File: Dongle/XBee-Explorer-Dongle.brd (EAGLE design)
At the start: 40.6 x 27.9 mm, 38 parts, among them U2 XBEE-1B3, U3 MIC5205 3.3V, U4 FT231XS

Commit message: Increasing fiducial size and LED footprint
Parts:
- removed LED1: Red, SparkFun:LED-0603
- removed LED2: Red-TX, SparkFun:LED-0603
- removed LED3: Green-RX, SparkFun:LED-0603
- removed LED4: Green, SparkFun:LED-0603
- added D1, D4: RED, SparkFun-LED:LED-0603
- added D2, D3: GREEN, SparkFun-LED:LED-0603
- FID1, FID2: value FIDUCIALUFIDUCIAL -> FIDUCIAL1X2; device SparkFun-Aesthetics:MICRO-FIDUCIAL -> SparkFun-Aesthetics:FIDUCIAL-1X2
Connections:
- net GND: now also D3.C, D4.C; no longer LED1.C, LED4.C
- net N$1: now also D1.A; no longer LED2.A
- net N$2: now also D3.A; no longer LED4.A
- net N$38: now also D4.A; no longer LED1.A
- net N$4: now also D2.A; no longer LED3.A
- net RXLED: now also D2.C; no longer LED3.C
- net TXLED: now also D1.C; no longer LED2.C
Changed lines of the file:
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@@
 <wire x1="0" y1="27.94" x2="40.64" y2="27.94" width="0.2032" layer="20"/>
 <wire x1="0" y1="0" x2="40.64" y2="0" width="0.2032" layer="20"/>
-<text x="7.62" y="17.272" size="1.016" layer="21" ratio="15">PWR</text>
-<text x="37.592" y="9.525" size="1.016" layer="21" ratio="15" align="center-right">TX</text>
-<text x="37.592" y="8.255" size="1.016" layer="21" ratio="15" align="center-right">RX</text>
-<text x="37.592" y="19.685" size="1.016" layer="21" ratio="15" align="center-right">RSSI</text>
+<text x="9.017" y="17.78" size="1.016" layer="21" ratio="15" align="center">PWR</text>
+<text x="37.338" y="9.525" size="1.016" layer="21" ratio="15" align="center-right">TX</text>
+<text x="37.338" y="8.255" size="1.016" layer="21" ratio="15" align="center-right">RX</text>
+<text x="37.338" y="19.685" size="1.016" layer="21" ratio="15" align="center-right">RSSI</text>
 <text x="33.528" y="20.066" size="1.016" layer="22" ratio="15" rot="MR270">3.3V</text>
 <text x="30.988" y="20.066" size="1.016" layer="22" ratio="15" rot="MR270">DOUT</text>
@@
 </class>
 </classes>
-<designrules name="SparkFun">
+<designrules name="SparkFun-2-layer">
 <description language="en">&lt;b&gt;EAGLE Design Rules&lt;/b&gt;
 &lt;p&gt;
@@
 <param name="dpGapFactor" value="2.5"/>
 <param name="checkGrid" value="0"/>
-<param name="checkAngle" value="0"/>
+<param name="checkAngle" value="1"/>
 <param name="checkFont" value="1"/>
 <param name="checkRestrict" value="1"/>
@@
 <attribute name="VALUE" x="19.8755" y="8.636" size="0.4064" layer="27"/>
 </element>
-<element name="LED1" library="SparkFun" package="LED-0603" value="Red" x="8.89" y="19.05" smashed="yes" rot="R90">
-<attribute name="NAME" x="9.779" y="18.3515" size="0.4064" layer="25" rot="R180"/>
-<attribute name="VALUE" x="10.287" y="18.3515" size="0.4064" layer="27"/>
-</element>
-<element name="LED2" library="SparkFun" package="LED-0603" value="Red-TX" x="38.735" y="9.525" smashed="yes" rot="R270">
-<attribute name="NAME" x="36.735" y="9.525" size="1.27" layer="25" rot="R180"/>
-<attribute name="VALUE" x="38.163" y="8.89" size="0.4064" layer="27" rot="R180"/>
-</element>
-<element name="LED3" library="SparkFun" package="LED-0603" value="Green-RX" x="38.735" y="8.255" smashed="yes" rot="R270">
-<attribute name="NAME" x="36.735" y="8.255" size="1.27" layer="25" rot="R180"/>
-<attribute name="VALUE" x="38.163" y="7.493" size="0.4064" layer="27" rot="R180"/>
-</element>
 <element name="R1" library="SparkFun" package="0603-RES" value="1K" x="31.75" y="10.414" smashed="yes">
 <attribute name="NAME" x="33.75" y="10.414" size="1.27" layer="25"/>
@@
 <element name="U$10" library="SparkFun" package="STAND-OFF" value="STAND-OFF" x="38.1" y="25.4"/>
 <element name="U$11" library="SparkFun" package="STAND-OFF" value="STAND-OFF" x="38.1" y="2.54"/>
-<element name="LED4" library="SparkFun" package="LED-0603" value="Green" x="38.735" y="19.685" smashed="yes" rot="R270">
-<attribute name="NAME" x="37.846" y="20.3835" size="0.4064" layer="25"/>
-<attribute name="VALUE" x="36.068" y="18.4785" size="0.4064" layer="27"/>
-</element>
 <element name="R4" library="SparkFun" package="0603-RES" value="330" x="22.86" y="19.05" smashed="yes" rot="R180">
 <attribute name="NAME" x="23.749" y="18.3515" size="0.4064" layer="25" rot="R180"/>
@@
 <element name="FRAME1" library="SparkFun-Aesthetics" package="CREATIVE_COMMONS" value="FRAME-LETTER" x="6.35" y="-8.89"/>
 <element name="U$7" library="SparkFun" package="OSHW-LOGO-S" value="OSHW-LOGOS" x="8.89" y="25.4"/>
-<element name="FID1" library="SparkFun-Aesthetics" package="MICRO-FIDUCIAL" value="FIDUCIALUFIDUCIAL" x="6.35" y="26.67"/>
-<element name="FID2" library="SparkFun-Aesthetics" package="MICRO-FIDUCIAL" value="FIDUCIALUFIDUCIAL" x="34.29" y="1.27"/>
-<element name="S2" library="SparkFun-Electromechanical" package="TACTILE_SWITCH_SMD" value="Reset" x="37.973" y="13.97" rot="R270"/>
+<element name="FID1" library="SparkFun-Aesthetics" package="FIDUCIAL-1X2" value="FIDUCIAL1X2" x="6.35" y="26.67"/>
+<element name="FID2" library="SparkFun-Aesthetics" package="FIDUCIAL-1X2" value="FIDUCIAL1X2" x="34.29" y="1.27"/>
+<element name="S2" library="SparkFun-Electromechanical" package="TACTILE_SWITCH_SMD" value="Reset" x="37.973" y="13.97" rot="R270">
+<attribute name="PROD_ID" value="SWCH-08247" x="37.973" y="13.97" size="1.778" layer="27" rot="R270" display="off"/>
+</element>
 <element name="U2" library="SparkFun-RF" package="XBEE-SMD" value="XBEE-1B3" x="11.43" y="13.97" rot="R270">
 <attribute name="PROD_ID" value="CONN-09042" x="11.43" y="13.97" size="1.27" layer="27" font="vector" ratio="15" rot="R270" display="off"/>
@@
 <element name="SJ3" library="SparkFun-Passives" package="SJ_2S-TRACE" value="RSSI" x="16.51" y="3.81" rot="MR0"/>
 <element name="SJ4" library="SparkFun-Passives" package="SJ_2S-TRACE" value="RSSI" x="13.97" y="24.13" rot="MR0"/>
+<element name="D1" library="SparkFun-LED" package="LED-0603" value="RED" x="38.735" y="9.525" rot="R270">
+<attribute name="PROD_ID" value="DIO-00819" x="38.735" y="9.525" size="1.778" layer="27" font="vector" ratio="15" rot="R270" display="off"/>
+</element>
+<element name="D2" library="SparkFun-LED" package="LED-0603" value="GREEN" x="38.735" y="8.255" rot="R270">
+<attribute name="PROD_ID" value="DIO-00821" x="38.735" y="8.255" size="1.778" layer="27" font="vector" ratio="15" rot="R270" display="off"/>
+</element>
+<element name="D3" library="SparkFun-LED" package="LED-0603" value="GREEN" x="38.735" y="19.685" rot="R270">
+<attribute name="PROD_ID" value="DIO-00821" x="38.735" y="19.685" size="1.778" layer="27" font="vector" ratio="15" rot="R270" display="off"/>
+</element>
+<element name="D4" library="SparkFun-LED" package="LED-0603" value="RED" x="8.89" y="19.05" rot="R90">
+<attribute name="PROD_ID" value="DIO-00819" x="8.89" y="19.05" size="1.778" layer="27" font="vector" ratio="15" rot="R90" display="off"/>
+</element>
 </elements>
 <signals>
@@
 <contactref element="C11" pad="2"/>
 <contactref element="C14" pad="2"/>
-<contactref element="LED1" pad="C"/>
-<contactref element="LED4" pad="C"/>
 <contactref element="U3" pad="2"/>
 <contactref element="C1" pad="C"/>
@@
 <contactref element="U2" pad="10"/>
 <contactref element="U2" pad="10"/>
+<contactref element="D4" pad="C"/>
+<contactref element="D3" pad="C"/>
 </signal>
 <signal name="RESET">
@@
 <signal name="N$38">
 <contactref element="R11" pad="1"/>
-<contactref element="LED1" pad="A"/>
-<wire x1="9.64" y1="19.05" x2="11.85" y2="19.05" width="0.254" layer="1"/>
+<contactref element="D4" pad="A"/>
+<wire x1="9.767" y1="19.05" x2="11.85" y2="19.05" width="0.254" layer="1"/>
 </signal>
 <signal name="N$1">
-<contactref element="LED2" pad="A"/>
 <contactref element="R1" pad="2"/>
 <wire x1="32.6" y1="10.414" x2="35.306" y2="10.414" width="0.254" layer="1"/>
 <wire x1="35.306" y1="10.414" x2="36.195" y2="9.525" width="0.254" layer="1"/>
-<wire x1="37.985" y1="9.525" x2="36.195" y2="9.525" width="0.254" layer="1"/>
+<contactref element="D1" pad="A"/>
+<wire x1="36.195" y1="9.525" x2="37.858" y2="9.525" width="0.254" layer="1"/>
 </signal>
 <signal name="N$4">
-<contactref element="LED3" pad="A"/>
 <contactref element="R3" pad="2"/>
 <wire x1="32.6" y1="8.636" x2="35.814" y2="8.636" width="0.254" layer="1"/>
 <wire x1="35.814" y1="8.636" x2="36.195" y2="8.255" width="0.254" layer="1"/>
-<wire x1="37.985" y1="8.255" x2="36.195" y2="8.255" width="0.254" layer="1"/>
+<contactref element="D2" pad="A"/>
+<wire x1="36.195" y1="8.255" x2="37.858" y2="8.255" width="0.254" layer="1"/>
 </signal>
 <signal name="DIN">
@@
 </signal>
 <signal name="TXLED">
-<contactref element="LED2" pad="C"/>
 <via x="38.1" y="11.43" extent="1-16" drill="0.508"/>
 <contactref element="U4" pad="10"/>
@@
 <wire x1="22.86" y1="15.24" x2="34.29" y2="15.24" width="0.254" layer="16"/>
 <wire x1="34.29" y1="15.24" x2="38.1" y2="11.43" width="0.254" layer="16"/>
-<wire x1="39.485" y1="9.525" x2="39.497" y2="10.033" width="0.254" layer="1"/>
-<wire x1="39.497" y1="10.033" x2="38.1" y2="11.43" width="0.254" layer="1"/>
+<contactref element="D1" pad="C"/>
+<wire x1="39.612" y1="9.525" x2="39.612" y2="9.918" width="0.254" layer="1"/>
+<wire x1="39.612" y1="9.918" x2="38.1" y2="11.43" width="0.254" layer="1"/>
 </signal>
 <signal name="RXLED">
-<contactref element="LED3" pad="C"/>
 <contactref element="U4" pad="17"/>
 <wire x1="23.8125" y1="11.2903" x2="23.8125" y2="10.6045" width="0.254" layer="1"/>
@@
 <wire x1="37.973" y1="7.747" x2="39.37" y2="6.35" width="0.254" layer="16"/>
 <via x="39.37" y="6.35" extent="1-16" drill="0.508"/>
-<wire x1="39.37" y1="6.35" x2="39.37" y2="8.14" width="0.254" layer="1"/>
-<wire x1="39.37" y1="8.14" x2="39.485" y2="8.255" width="0.254" layer="1"/>
+<contactref element="D2" pad="C"/>
+<wire x1="39.612" y1="8.255" x2="39.612" y2="7.481" width="0.254" layer="1"/>
+<wire x1="39.612" y1="7.481" x2="39.37" y2="7.239" width="0.254" layer="1"/>
+<wire x1="39.37" y1="7.239" x2="39.37" y2="6.35" width="0.254" layer="1"/>
 </signal>
 <signal name="DIO4">
@@
 </signal>
 <signal name="N$2">
-<contactref element="LED4" pad="A"/>
 <contactref element="R4" pad="1"/>
 <wire x1="23.71" y1="19.05" x2="24.511" y2="19.05" width="0.254" layer="1"/>
@@
 <via x="28.829" y="19.939" extent="1-16" drill="0.508"/>
 <via x="37.973" y="20.955" extent="1-16" drill="0.508"/>
-<wire x1="37.985" y1="19.685" x2="37.973" y2="20.955" width="0.254" layer="1"/>
 <wire x1="28.829" y1="19.939" x2="36.957" y2="19.939" width="0.254" layer="16"/>
 <wire x1="36.957" y1="19.939" x2="37.973" y2="20.955" width="0.254" layer="16"/>
+<contactref element="D3" pad="A"/>
+<wire x1="37.858" y1="19.685" x2="37.858" y2="20.84" width="0.254" layer="1"/>
+<wire x1="37.858" y1="20.84" x2="37.973" y2="20.955" width="0.254" layer="1"/>
 </signal>
 <signal name="3V-INT" class="1">

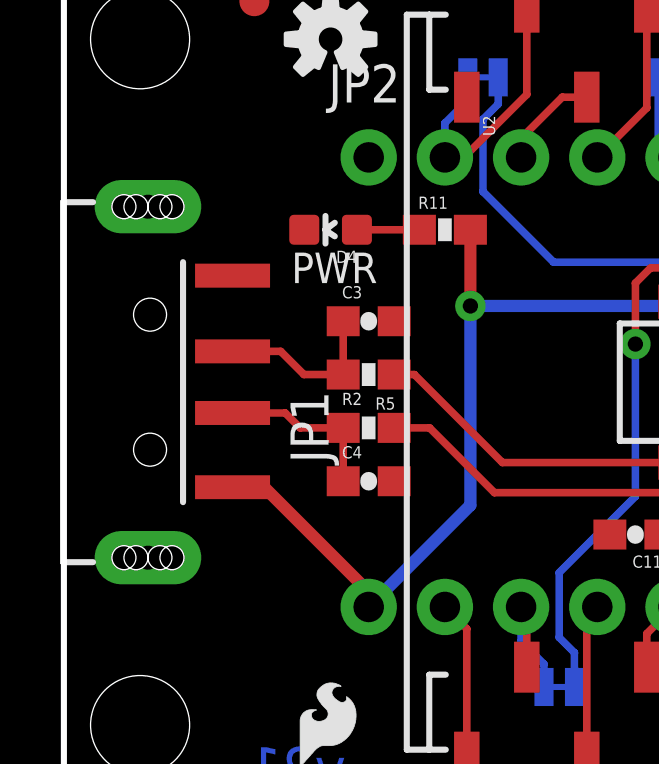
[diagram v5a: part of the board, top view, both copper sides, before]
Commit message: Moving USB connector back a bit to hold in place
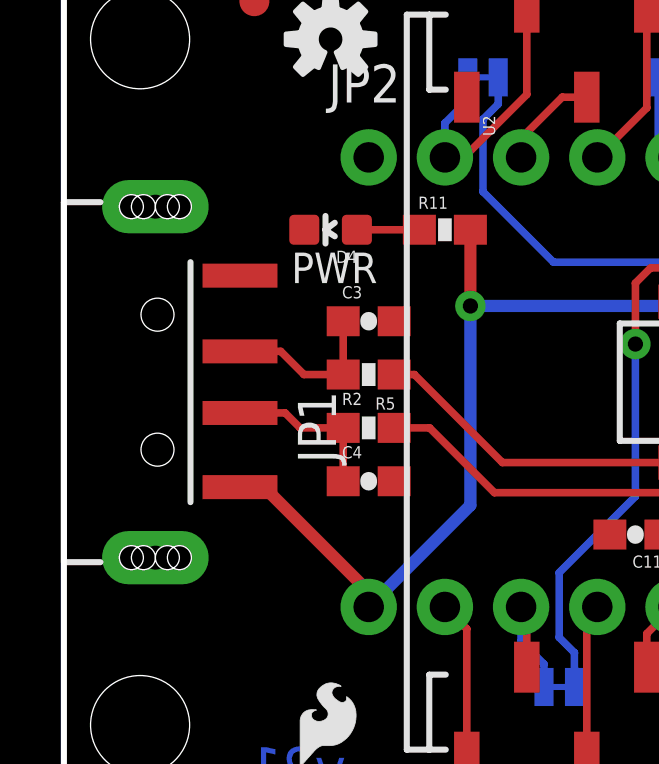
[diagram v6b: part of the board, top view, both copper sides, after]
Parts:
- moved JP1 2.54 mm to (0.00, 14.0)
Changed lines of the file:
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@@
 <layer number="47" name="Measures" color="7" fill="1" visible="no" active="yes"/>
 <layer number="48" name="Document" color="7" fill="1" visible="no" active="yes"/>
-<layer number="49" name="Reference" color="7" fill="1" visible="yes" active="yes"/>
+<layer number="49" name="Reference" color="7" fill="1" visible="no" active="yes"/>
 <layer number="50" name="dxf" color="7" fill="1" visible="no" active="yes"/>
 <layer number="51" name="tDocu" color="6" fill="1" visible="yes" active="yes"/>
@@
 <layer number="108" name="tplace-old" color="10" fill="1" visible="no" active="yes"/>
 <layer number="109" name="ref-old" color="11" fill="1" visible="no" active="yes"/>
+<layer number="110" name="fp0" color="7" fill="1" visible="yes" active="yes"/>
+<layer number="111" name="LPC17xx" color="7" fill="1" visible="yes" active="yes"/>
+<layer number="112" name="tSilk" color="7" fill="1" visible="yes" active="yes"/>
+<layer number="113" name="IDFDebug" color="4" fill="1" visible="yes" active="yes"/>
 <layer number="116" name="Patch_BOT" color="9" fill="4" visible="no" active="yes"/>
 <layer number="121" name="_tsilk" color="7" fill="1" visible="no" active="yes"/>
 <layer number="122" name="_bsilk" color="7" fill="1" visible="no" active="yes"/>
+<layer number="123" name="tTestmark" color="7" fill="1" visible="yes" active="yes"/>
+<layer number="124" name="bTestmark" color="7" fill="1" visible="yes" active="yes"/>
 <layer number="125" name="_tNames" color="7" fill="1" visible="no" active="yes"/>
+<layer number="126" name="_bNames" color="7" fill="1" visible="yes" active="yes"/>
+<layer number="127" name="_tValues" color="7" fill="1" visible="yes" active="yes"/>
+<layer number="128" name="_bValues" color="7" fill="1" visible="yes" active="yes"/>
+<layer number="131" name="tAdjust" color="7" fill="1" visible="yes" active="yes"/>
+<layer number="132" name="bAdjust" color="7" fill="1" visible="yes" active="yes"/>
 <layer number="144" name="Drill_legend" color="7" fill="1" visible="no" active="yes"/>
 <layer number="151" name="HeatSink" color="7" fill="1" visible="no" active="yes"/>
+<layer number="152" name="_bDocu" color="7" fill="1" visible="yes" active="yes"/>
 <layer number="199" name="Contour" color="7" fill="1" visible="no" active="yes"/>
 <layer number="200" name="200bmp" color="1" fill="10" visible="no" active="no"/>
@@
 <layer number="223" name="223bmp" color="24" fill="1" visible="no" active="no"/>
 <layer number="224" name="224bmp" color="25" fill="1" visible="no" active="no"/>
+<layer number="248" name="Housing" color="7" fill="1" visible="yes" active="yes"/>
+<layer number="249" name="Edge" color="7" fill="1" visible="yes" active="yes"/>
 <layer number="250" name="Descript" color="3" fill="1" visible="no" active="no"/>
 <layer number="251" name="SMDround" color="12" fill="11" visible="no" active="no"/>
@@
 <element name="JP2" library="SparkFun" package="1X11_NO_SILK" value="M111X11_NO_SILK" x="10.16" y="21.463"/>
 <element name="U$8" library="SparkFun" package="OSHW-LOGO-S" value="OSHW-LOGOS" x="10.16" y="13.97" rot="MR0"/>
-<element name="JP1" library="SparkFun-Connectors" package="USB-A-SMT-MALE" value="USBA-SMD-MALE" x="2.54" y="13.97" rot="R90"/>
+<element name="JP1" library="SparkFun-Connectors" package="USB-A-SMT-MALE" value="USBA-SMD-MALE" x="0" y="13.97" rot="R90"/>
 <element name="U4" library="SparkFun-DigitalIC" package="SSOP20_L" value="FT231XS" x="22.86" y="13.97" rot="R180"/>
 <element name="R2" library="SparkFun" package="0603-RES" value="27" x="10.16" y="12.446"/>
@@
 <wire x1="22.01" y1="9.564" x2="22.5425" y2="10.0965" width="0.254" layer="1"/>
 <wire x1="22.5425" y1="11.2903" x2="22.5425" y2="10.0965" width="0.254" layer="1"/>
-<wire x1="5.6218" y1="10.47" x2="6.675" y2="10.47" width="0.4064" layer="1"/>
+<wire x1="5.87" y1="10.47" x2="6.675" y2="10.47" width="0.4064" layer="1"/>
 <wire x1="6.675" y1="10.47" x2="10.16" y2="6.985" width="0.4064" layer="1"/>
 <wire x1="10.16" y1="6.985" x2="10.16" y2="6.477" width="0.4064" layer="1"/>
@@
 <contactref element="R2" pad="1"/>
 <contactref element="C4" pad="1"/>
-<wire x1="5.6218" y1="12.943" x2="7.377" y2="12.943" width="0.254" layer="1"/>
+<wire x1="5.87" y1="12.943" x2="7.377" y2="12.943" width="0.254" layer="1"/>
 <wire x1="7.377" y1="12.943" x2="7.874" y2="12.446" width="0.254" layer="1"/>
 <wire x1="7.874" y1="12.446" x2="9.31" y2="12.446" width="0.254" layer="1"/>
@@
 <contactref element="C3" pad="1"/>
 <wire x1="9.31" y1="14.224" x2="9.31" y2="16.002" width="0.254" layer="1"/>
-<wire x1="5.6218" y1="14.997" x2="7.228" y2="14.997" width="0.254" layer="1"/>
+<wire x1="5.87" y1="14.997" x2="7.228" y2="14.997" width="0.254" layer="1"/>
 <wire x1="7.228" y1="14.997" x2="8.001" y2="14.224" width="0.254" layer="1"/>
 <wire x1="8.001" y1="14.224" x2="9.31" y2="14.224" width="0.254" layer="1"/>
